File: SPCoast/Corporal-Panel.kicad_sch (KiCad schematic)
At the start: 16 parts, among them U12031 0x2A, U12032 0x2B

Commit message: refactor(kicad): seam vocabulary after the naming audit: Processor, IOBus, PanelIOBus, House, Style, TimeCode, LocoNet, NodeType, MQTT-JMRI
SPCoast/edits/2026-10-22-vocabulary.py, the owner's rulings on
FieldUnit-Subdivision docs/review/naming-audit-2026-10-22.md:
- Host stays only on the transport symbols; the Interlocking, OfficeUnit and Processor pins, the unit
  sheets' port and labels are Processor.
- IOBus on the Processor pin; the office side is PanelIOBus on the unit ports, the Panel boxes' pins,
  the panel labels and the root sheet pins.
- MAIN HOUSE is House; its H pin is MC and hidden, as asked.
- OfficeUnit Type -> Style = US&S; TimeCode and LocoNet spellings, the LocoNet transport's pin is
  Transport; the one input Codeline sheet pin is bidirectional.
- The CMRInet node's Board -> NodeType (body text follows); JMRI drivers' IC = MQTT-JMRI.

Verified: --check on production/vocab-before.net vs vocab-after.net: identical connectivity under the
pin map, same parts (MAIN HOUSE -> House), only the ruled fields changed; field-io --check passes;
ERC 0 violations.

Co-Authored-By: Claude Fable 5.1 <noreply@anthropic.com>
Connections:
- net IOBus renamed PanelIOBus
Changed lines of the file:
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@@
 		(at 138.43 77.47)
 	)
-	(hierarchical_label "IOBus"
+	(hierarchical_label "PanelIOBus"
 		(shape bidirectional)
 		(at 162.56 111.76 0)
@@
 		)
 	)
-	(hierarchical_label "IOBus"
+	(hierarchical_label "PanelIOBus"
 		(shape bidirectional)
 		(at 111.76 111.76 0)

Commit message: refactor(kicad): model board lamps leave the columns; stale instance fields follow the libraries; PanelLamp-* retired
The owner's ruling (2026-10-23): the PanelColumn is the logical column, tied to a control point; the panel
I/O hardware is not. Every PanelLamp was a model board lamp except the maintainer-call lamp on the column's
pin 8. 34 lamps are now ModelLamp-<color> (no Column pin, Style board); 8 MC lamps are PanelMCall-Lamp.
Wires untouched: ~{LAMP} keeps its pin and the Column wire of a model lamp ends on nothing. Instance fields
the libraries dropped in c1d446b are gone from the sheets: Address on 7 processors, Interlocking and Machine
on 14 columns, Host on 2 transports. Railroad stays on the AAR encoding because its Topic template reads
${Railroad}; where Railroad lives is pending. Cached definitions refreshed for Processor, PanelColumn,
Transport-MQTT and Encoding-AAR. Scripted: SPCoast/edits/2026-10-23-model-lamps.py (edit, --check, --retire).

Verified: the script's gate on production/fields-after.net vs model-lamps-after.net: same 743 parts, lib ids
change only on the 42 lamps to the expected targets, fields change only as listed (Style indication->board
x34, the 37 drops), connectivity after == before minus the model lamps' pin 1, ERC 0 violations (the two
lib_symbol_mismatch warnings gone). lint_symbol_fields: 97 symbols, 0 errors (PanelLamp-BLUE, -GREEN, -RED, -YELLOW retired; there was no AMBER). Subdivision tests: 157 OK.

Co-Authored-By: Claude Fable 5.1 <noreply@anthropic.com>
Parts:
- COL12031, COL12032: Interlocking Corporal -> (none); Machine SPCoast South -> (none)
- LMP12111, LMP12113, LMP12123: symbol Railroad-Office:PanelLamp-YELLOW -> Railroad-Office:ModelLamp-YELLOW; Style indication -> board
- LMP12112: symbol Railroad-Office:PanelLamp-RED -> Railroad-Office:ModelLamp-RED; Style indication -> board
- LMP12121, LMP12122: symbol Railroad-Office:PanelLamp-BLUE -> Railroad-Office:ModelLamp-BLUE; Style indication -> board
- MCK12011: symbol Railroad-Office:PanelLamp-YELLOW -> Railroad-Office:PanelMCall-Lamp
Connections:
- net at COL12031.1 (Column): no longer LMP12111.1 (Column)
- net at COL12032.3 (Column): no longer LMP12123.1 (Column)
- net at COL12031.3 (Column): no longer LMP12113.1 (Column)
- net at COL12032.1 (Column): no longer LMP12121.1 (Column)
- net at COL12032.2 (Column): no longer LMP12122.1 (Column)
- net at COL12031.2 (Column): no longer LMP12112.1 (Column)
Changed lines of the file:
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@@
 	)
 	(symbol
-		(lib_id "Railroad-Office:PanelLamp-YELLOW")
+		(lib_id "Railroad-Office:ModelLamp-YELLOW")
 		(at 80.01 26.67 0)
 		(unit 1)
@@
 			)
 		)
-		(property "Description" "One physical model board lamp. Value is a free descriptive label (e.g. OS, TRACK, MC) and is not used elsewhere. IndicationToken is a comma-separated list of indication names (track circuits such as 795T1,2NAA,799T1, or tokens such as MC1K) OR'd to drive this one lamp. All listed indications are still individually on the CodeLine wire"
+		(property "Description" "One physical model board lamp. Value is a free descriptive label (e.g. OS, TRACK ...) and is not used elsewhere. IndicationToken is a comma-separated list of indication names (tokens from the CodeLine) OR'd to drive this one lamp."
 			(at 80.01 34.29 0)
 			(hide yes)
@@
 			)
 		)
-		(property "Style" "indication"
+		(property "Style" "board"
 			(at 80.01 24.13 0)
 			(hide yes)
@@
 				)
 			)
-		)
-		(pin "1"
 		)
 		(pin "2"
@@
 	)
 	(symbol
-		(lib_id "Railroad-Office:PanelLamp-YELLOW")
+		(lib_id "Railroad-Office:ModelLamp-YELLOW")
 		(at 130.81 36.83 0)
 		(unit 1)
@@
 			)
 		)
-		(property "Description" "One physical model board lamp. Value is a free descriptive label (e.g. OS, TRACK, MC) and is not used elsewhere. IndicationToken is a comma-separated list of indication names (track circuits such as 795T1,2NAA,799T1, or tokens such as MC1K) OR'd to drive this one lamp. All listed indications are still individually on the CodeLine wire"
+		(property "Description" "One physical model board lamp. Value is a free descriptive label (e.g. OS, TRACK ...) and is not used elsewhere. IndicationToken is a comma-separated list of indication names (tokens from the CodeLine) OR'd to drive this one lamp."
 			(at 130.81 44.45 0)
 			(hide yes)
@@
 			)
 		)
-		(property "Style" "indication"
+		(property "Style" "board"
 			(at 130.81 34.29 0)
 			(hide yes)
@@
 				)
 			)
-		)
-		(pin "1"
 		)
 		(pin "2"
@@
 	)
 	(symbol
-		(lib_id "Railroad-Office:PanelLamp-YELLOW")
+		(lib_id "Railroad-Office:ModelLamp-YELLOW")
 		(at 80.01 36.83 0)
 		(unit 1)
@@
 			)
 		)
-		(property "Description" "One physical model board lamp. Value is a free descriptive label (e.g. OS, TRACK, MC) and is not used elsewhere. IndicationToken is a comma-separated list of indication names (track circuits such as 795T1,2NAA,799T1, or tokens such as MC1K) OR'd to drive this one lamp. All listed indications are still individually on the CodeLine wire"
+		(property "Description" "One physical model board lamp. Value is a free descriptive label (e.g. OS, TRACK ...) and is not used elsewhere. IndicationToken is a comma-separated list of indication names (tokens from the CodeLine) OR'd to drive this one lamp."
 			(at 80.01 44.45 0)
 			(hide yes)
@@
 			)
 		)
-		(property "Style" "indication"
+		(property "Style" "board"
 			(at 80.01 34.29 0)
 			(hide yes)
@@
 				)
 			)
-		)
-		(pin "1"
 		)
 		(pin "2"
@@
 	)
 	(symbol
-		(lib_id "Railroad-Office:PanelLamp-YELLOW")
+		(lib_id "Railroad-Office:PanelMCall-Lamp")
 		(at 80.01 104.14 0)
 		(unit 1)
@@
 			)
 		)
-		(property "Description" "One physical model board lamp. Value is a free descriptive label (e.g. OS, TRACK, MC) and is not used elsewhere. IndicationToken is a comma-separated list of indication names (track circuits such as 795T1,2NAA,799T1, or tokens such as MC1K) OR'd to drive this one lamp. All listed indications are still individually on the CodeLine wire"
+		(property "Description" "One physical Maintainer Call lamp.  IndicationToken is a comma-separated list of indication names (tokens such as MC1K)"
 			(at 80.01 111.76 0)
 			(hide yes)
@@
 	)
 	(symbol
-		(lib_id "Railroad-Office:PanelLamp-BLUE")
+		(lib_id "Railroad-Office:ModelLamp-BLUE")
 		(at 130.81 26.67 0)
 		(unit 1)
@@
 			)
 		)
-		(property "Description" "One physical model board lamp. Value is a free descriptive label (e.g. OS, TRACK, MC) and is not used elsewhere. IndicationToken is a comma-separated list of indication names (track circuits such as 795T1,2NAA,799T1, or tokens such as MC1K) OR'd to drive this one lamp. All listed indications are still individually on the CodeLine wire"
+		(property "Description" "One physical model board lamp. Value is a free descriptive label (e.g. OS, TRACK ...) and is not used elsewhere. IndicationToken is a comma-separated list of indication names (tokens from the CodeLine) OR'd to drive this one lamp."
 			(at 130.175 36.195 0)
 			(hide yes)
@@
 			)
 		)
-		(property "Style" "indication"
+		(property "Style" "board"
 			(at 130.81 29.21 0)
 			(hide yes)
@@
 				)
 			)
-		)
-		(pin "1"
 		)
 		(pin "2"
@@
 	)
 	(symbol
-		(lib_id "Railroad-Office:PanelLamp-BLUE")
+		(lib_id "Railroad-Office:ModelLamp-BLUE")
 		(at 130.81 31.75 0)
 		(unit 1)
@@
 			)
 		)
-		(property "Description" "One physical model board lamp. Value is a free descriptive label (e.g. OS, TRACK, MC) and is not used elsewhere. IndicationToken is a comma-separated list of indication names (track circuits such as 795T1,2NAA,799T1, or tokens such as MC1K) OR'd to drive this one lamp. All listed indications are still individually on the CodeLine wire"
+		(property "Description" "One physical model board lamp. Value is a free descriptive label (e.g. OS, TRACK ...) and is not used elsewhere. IndicationToken is a comma-separated list of indication names (tokens from the CodeLine) OR'd to drive this one lamp."
 			(at 130.175 41.275 0)
 			(hide yes)
@@
 			)
 		)
-		(property "Style" "indication"
+		(property "Style" "board"
 			(at 130.81 34.29 0)
 			(hide yes)
@@
 				)
 			)
-		)
-		(pin "1"
 		)
 		(pin "2"
@@
 	)
 	(symbol
-		(lib_id "Railroad-Office:PanelLamp-RED")
+		(lib_id "Railroad-Office:ModelLamp-RED")
 		(at 80.01 31.75 0)
 		(unit 1)
@@
 			)
 		)
-		(property "Description" "One physical model board lamp. Value is a free descriptive label (e.g. OS, TRACK, MC) and is not used elsewhere. IndicationToken is a comma-separated list of indication names (track circuits such as 795T1,2NAA,799T1, or tokens such as MC1K) OR'd to drive this one lamp. All listed indications are still individually on the CodeLine wire"
+		(property "Description" "One physical model board lamp. Value is a free descriptive label (e.g. OS, TRACK ...) and is not used elsewhere. IndicationToken is a comma-separated list of indication names (tokens from the CodeLine) OR'd to drive this one lamp."
 			(at 79.375 41.275 0)
 			(hide yes)
@@
 			)
 		)
-		(property "Style" "indication"
+		(property "Style" "board"
 			(at 80.01 34.29 0)
 			(hide yes)
@@
 				)
 			)
-		)
-		(pin "1"
 		)
 		(pin "2"
@@
 			)
 		)
-		(property "Interlocking" "Corporal"
-			(at 80.01 129.54 0)
-			(show_name yes)
-			(do_not_autoplace yes)
-			(effects
-				(font
-					(size 1.27 1.27)
-				)
-			)
-		)
-		(property "Machine" "SPCoast South"
-			(at 80.645 125.73 0)
-			(show_name no)
-			(do_not_autoplace yes)
-			(effects
-				(font
-					(size 1.905 1.905)
-				)
-			)
-		)
 		(property "Role" "COLUMN"
 			(at 80.645 122.555 0)
@@
 				)
 			)
-		)
-		(property "Interlocking" "Corporal"
-			(at 130.81 129.54 0)
-			(show_name yes)
-			(do_not_autoplace yes)
-			(effects
-				(font
-					(size 1.27 1.27)
-				)
-			)
-		)
-		(property "Machine" "SPCoast South"
-			(at 131.445 125.73 0)
-			(show_name no)
-			(do_not_autoplace yes)
-			(effects
-				(font
-					(size 1.905 1.905)
-				)
-			)

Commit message: refactor(kicad): Name on every device, office unit and encoding; Kind on the JMRI drivers; Driver-JMRI-Light
The owner's rulings of 2026-10-24 on the review of ADR 0008 rev 4: Name = ${Value}
is the identity key everywhere, devices included; the OfficeUnit's Columns is
derived and struck; a JMRI driver carries no address and is keyed by its object
class and the device it serves, the class carried by Kind (TURNOUT, SENSOR,
SIGNALMAST, LIGHT); Driver-JMRI-Light (ADR 0005 §8: ON, INTENSITY) for a lamp
JMRI drives, and the two Gilroy Interchange maintainer-call lamps MC1 and MC2
become Lights (they were Sensors, which JMRI only displays).

Script: SPCoast/edits/2026-10-24-names-kind-light.py. Libraries: Name on 36
symbols (OfficeUnit, 5 encodings, 12 PANEL, 18 DEVICE), Columns off OfficeUnit,
Kind on 5 JMRI drivers, Driver-JMRI-Light added (the Sensor's pin positions,
INTENSITY as pin 3 below, no-connect on the two placed instances). Sheets: 359
Name instance fields, 16 Kind, 2 lib_id swaps, caches refreshed (no pin moved on
a refreshed symbol).

Verified: gate --check production/SPCoast.net production/names-after.net PASS:
same parts, same connectivity, Name == Value on all 273 named instances (47
heads with Value "~" resolve to an empty Name), Columns dropped once, Kind on 16
drivers, 2 Sensor -> Light with pin 1 reading ON; ERC 0 before and after.
Subdivision lint_symbol_fields: 99 symbols, 0 errors (Kind now allowed on
IODRIVER). production/SPCoast.net is the new export (production/ is untracked).

Co-Authored-By: Claude Fable 5.1 <noreply@anthropic.com>
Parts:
- CDE12012, LKL12011, LMP12111, LMP12112, LMP12113, LMP12121, LMP12122, LMP12123, MCK12011, MCL12011, SGL12011, SWL12012: Name (none) -> ${Value}
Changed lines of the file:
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@@
 			)
 		)
+		(property "Name" "${Value}"
+			(at 80.01 26.67 0)
+			(hide yes)
+			(show_name no)
+			(do_not_autoplace no)
+			(effects
+				(font
+					(size 1.27 1.27)
+				)
+			)
+		)
 		(property "Appliance" "lamp"
 			(at 80.01 24.13 0)
@@
 			)
 		)
+		(property "Name" "${Value}"
+			(at 130.81 36.83 0)
+			(hide yes)
+			(show_name no)
+			(do_not_autoplace no)
+			(effects
+				(font
+					(size 1.27 1.27)
+				)
+			)
+		)
 		(property "Appliance" "lamp"
 			(at 130.81 34.29 0)
@@
 			)
 		)
+		(property "Name" "${Value}"
+			(at 80.01 36.83 0)
+			(hide yes)
+			(show_name no)
+			(do_not_autoplace no)
+			(effects
+				(font
+					(size 1.27 1.27)
+				)
+			)
+		)
 		(property "Appliance" "lamp"
 			(at 80.01 34.29 0)
@@
 			)
 		)
+		(property "Name" "${Value}"
+			(at 80.01 104.14 0)
+			(hide yes)
+			(show_name no)
+			(do_not_autoplace no)
+			(effects
+				(font
+					(size 1.27 1.27)
+				)
+			)
+		)
 		(property "Appliance" "lamp"
 			(at 80.01 101.6 0)
@@
 			)
 		)
+		(property "Name" "${Value}"
+			(at 130.81 26.67 0)
+			(hide yes)
+			(show_name no)
+			(do_not_autoplace no)
+			(effects
+				(font
+					(size 1.27 1.27)
+				)
+			)
+		)
 		(property "Appliance" "lamp"
 			(at 130.81 29.21 0)
@@
 			)
 		)
+		(property "Name" "${Value}"
+			(at 130.81 63.5 0)
+			(hide yes)
+			(show_name no)
+			(do_not_autoplace no)
+			(effects
+				(font
+					(size 1.27 1.27)
+				)
+			)
+		)
 		(property "Appliance" "lever"
 			(at 131.445 76.2 0)
@@
 			)
 		)
+		(property "Name" "${Value}"
+			(at 80.01 83.82 0)
+			(hide yes)
+			(show_name no)
+			(do_not_autoplace no)
+			(effects
+				(font
+					(size 1.27 1.27)
+				)
+			)
+		)
 		(property "Appliance" "lever"
 			(at 80.01 92.71 0)
@@
 			)
 		)
+		(property "Name" "${Value}"
+			(at 130.81 31.75 0)
+			(hide yes)
+			(show_name no)
+			(do_not_autoplace no)
+			(effects
+				(font
+					(size 1.27 1.27)
+				)
+			)
+		)
 		(property "Appliance" "lamp"
 			(at 130.81 34.29 0)
@@
 			)
 		)
+		(property "Name" "${Value}"
+			(at 130.81 63.5 0)
+			(hide yes)
+			(show_name no)
+			(do_not_autoplace no)
+			(effects
+				(font
+					(size 1.27 1.27)
+				)
+			)
+		)
 		(property "Appliance" "lever"
 			(at 131.445 76.2 0)
@@
 			)
 		)
+		(property "Name" "${Value}"
+			(at 80.01 31.75 0)
+			(hide yes)
+			(show_name no)
+			(do_not_autoplace no)
+			(effects
+				(font
+					(size 1.27 1.27)
+				)
+			)
+		)
 		(property "Appliance" "lamp"
 			(at 80.01 34.29 0)
@@
 			)
 		)
+		(property "Name" "${Value}"
+			(at 80.01 63.5 0)
+			(hide yes)
+			(show_name no)
+			(do_not_autoplace no)
+			(effects
+				(font
+					(size 1.27 1.27)
+				)
+			)
+		)
 		(property "Appliance" "lever"
 			(at 80.645 74.93 0)
@@
 			)
 		)
+		(property "Name" "${Value}"
+			(at 80.01 63.5 0)
+			(hide yes)
+			(show_name no)
+			(do_not_autoplace no)
+			(effects
+				(font
+					(size 1.27 1.27)
+				)
+			)
+		)
 		(property "Appliance" "lever"
 			(at 80.645 74.93 0)
@@
 			)
 		)
+		(property "Name" "${Value}"
+			(at 80.01 48.26 0)
+			(hide yes)
+			(show_name no)
+			(do_not_autoplace no)
+			(effects
+				(font
+					(size 1.27 1.27)
+				)
+			)
+		)
 		(property "Appliance" "lever"
 			(at 86.36 44.45 0)
@@
 			)
 		)
+		(property "Name" "${Value}"
+			(at 80.01 83.82 0)
+			(hide yes)
+			(show_name no)
+			(do_not_autoplace no)
+			(effects
+				(font
+					(size 1.27 1.27)
+				)
+			)
+		)
 		(property "Appliance" "lever"
 			(at 80.01 92.71 0)
@@
 			(hide yes)
 			(show_name no)
+			(do_not_autoplace no)
+			(effects
+				(font
+					(size 1.27 1.27)
+				)
+			)
+		)
+		(property "Name" "${Value}"
+			(at 130.81 97.79 0)
+			(hide yes)
+			(show_name no)

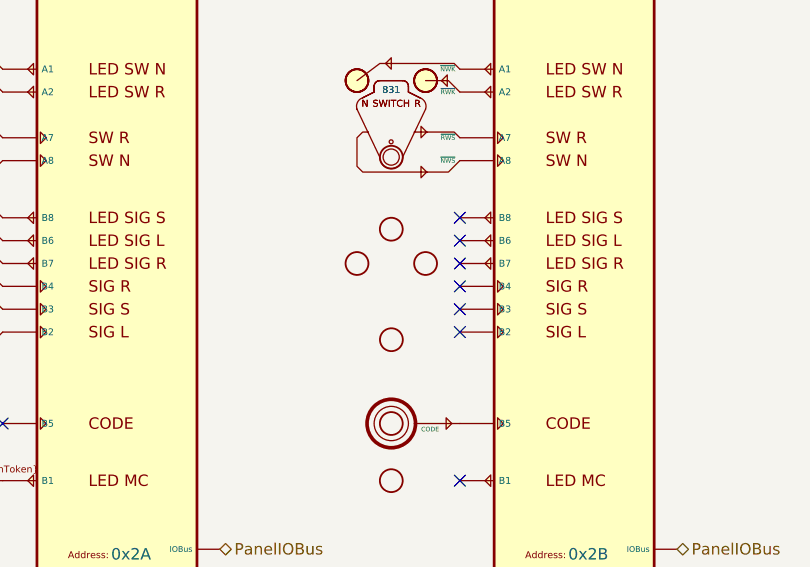
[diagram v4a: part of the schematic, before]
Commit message: feat(kicad): owner edit (2026-10-27): Gilroy Caltrain loses its maintainer call; Corporal gets lever 832
Gilroy Caltrain's field has no maintainer call, so the owner removed the MC1
lever and the MC lamp (MCK4001, IndicationToken MC1K) from its desk column. The
owner also added a signal lever for 832 to Corporal's desk (column 12), because
Corporal's field sends 832's indications and the desk had no lever for them.

Verified: a fresh kicad-cli export compiles with the reference derivation on
FieldUnit-Subdivision feat/derive with 0 errors, 0 warnings, 8 info and 16
missing. Corporal's controls include 832HS, 832NGS and 832SGS, and every
Corporal desk device is in its column. KiCad was closed (no lock files).

Co-Authored-By: Claude Opus 5.5 <noreply@anthropic.com>
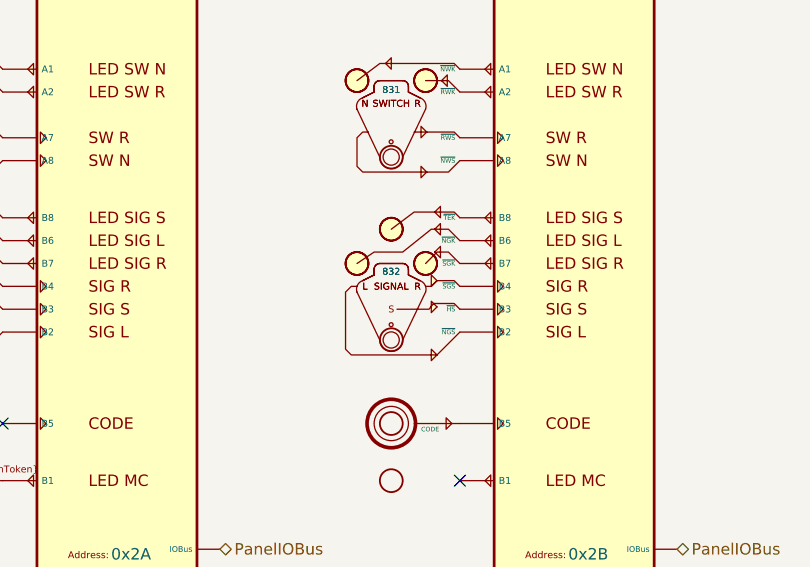
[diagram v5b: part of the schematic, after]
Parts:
- added SGL12012: 832, symbol Railroad-Office:PanelSignal
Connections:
- net at U12032.10 (B2): now also SGL12012.2 (~{NGS})
- net at U12032.11 (B3): now also SGL12012.3 (~{HS})
- net at U12032.12 (B4): now also SGL12012.4 (~{SGS})
- net at U12032.14 (B6): now also SGL12012.6 (~{NGK})
- net at U12032.15 (B7): now also SGL12012.5 (~{SGK})
- net at U12032.16 (B8): now also SGL12012.7 (~{TEK})
- net at COL12032.6 (Column): now also SGL12012.1 (Column)
- no-connect marks 9 -> 3

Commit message: feat(spcoast): every desk column names its CP Name
The owner's edit in KiCad: each PanelColumn carries a CP Name. On an
AAR codeline it may name the interlocking (Christopher, Gilroy
Interchange); on the 506 it names the house.

Verified: a fresh kicad-cli netlist compiles with no column.cp_name
diagnostics; the three column.house errors (columns 3, 4, 9) are
resolved by the importer rule, not the drawing.

Co-Authored-By: Claude Opus 5.5 <noreply@anthropic.com>
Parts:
- COL12031, COL12032: CP Name (none) -> Corporal
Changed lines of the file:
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@@
 			)
 		)
-		(property "CP Name" ""
+		(property "CP Name" "Corporal"
 			(at 80.645 132.08 0)
 			(show_name yes)
@@
 			)
 		)
-		(property "CP Name" ""
+		(property "CP Name" "Corporal"
 			(at 131.445 132.08 0)
 			(show_name yes)
